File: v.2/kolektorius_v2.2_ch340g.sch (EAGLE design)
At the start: 87 parts, among them IC1 LM1117-33, IC2 ENC28J60, K1 G5V1, K2 G5V1, K3 G5V1, T1 2N2222, T2 2N2222, T3 2N2222, T4 2N2222, U1 ATMEGA328P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

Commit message: Paliktos 2 reles
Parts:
- removed D1: (no value), adafruit:DIODEDO-1N4148
- removed K1: G5V1, relay:G5V1
- removed LED1: (no value), adafruit:LEDSMT1206
- removed R5: 470, rcl:R-EU_R0805
- removed R6: 3k3, rcl:R-EU_R0805
- removed T2: 2N2222, adafruit:2N2222
- removed X8: 22-23-2031, con-molex:22-23-2031
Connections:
- net D+ renamed N$15
- net D- renamed N$11
- removed net D0: R6.2, U1.PD0(RXD)
- removed net N$11 (its old number): D1.A, K11.2, R5.2, T2.C
- removed net N$15 (its old number): K12.S, X8-1.S
- removed net N$17: R6.1, T2.B
- removed net N$28: K12.P, K12.P@1, X8-3.S
- removed net N$29: K12.O, X8-2.S
- removed net N$31: LED1.C, R5.1
- removed net N$51: U$2.RXD
- new net RXD: U1.PD0(RXD)
- new net TXD: U$2.RXD, U1.PD1(TXD)
- net +5V: no longer D1.C, K11.1, LED1.A
- net D1: no longer U1.PD1(TXD)
- net GND: no longer T2.E
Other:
- moved on the sheet: C13, C15, C17, USB

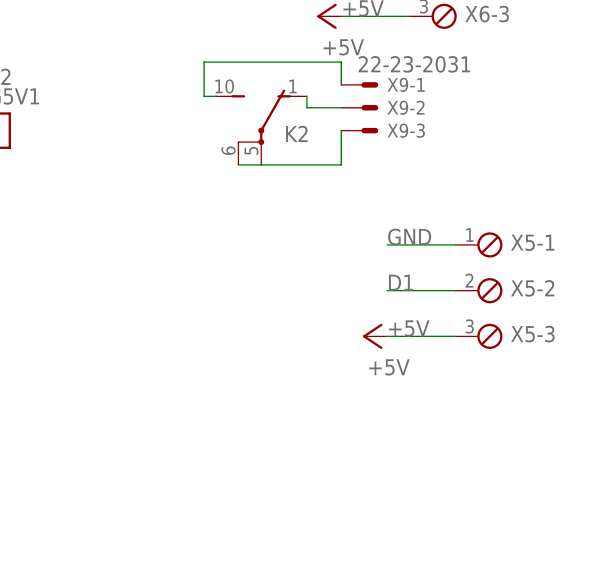
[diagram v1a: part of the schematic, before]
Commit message: pataisymai, paliktos 2 reles
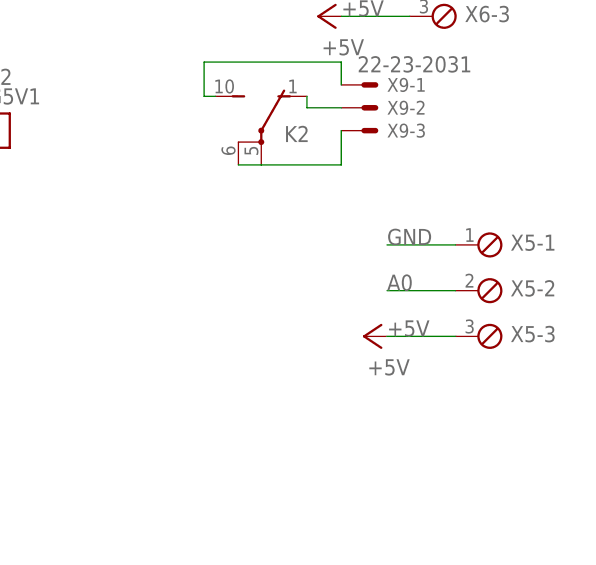
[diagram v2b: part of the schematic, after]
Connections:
- removed net D1: X5-2.1
- net A0: now also X5-2.1
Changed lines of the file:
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@@
 <label x="213.36" y="113.03" size="1.778" layer="95"/>
+</segment>
+<segment>
+<pinref part="X5" gate="-2" pin="1"/>
+<wire x1="313.69" y1="5.08" x2="306.07" y2="5.08" width="0.1524" layer="91"/>
+<label x="306.07" y="5.08" size="1.778" layer="95"/>
 </segment>
 </net>
@@
 </segment>
 </net>
-<net name="D1" class="0">
-<segment>
-<pinref part="X5" gate="-2" pin="1"/>
-<wire x1="313.69" y1="5.08" x2="306.07" y2="5.08" width="0.1524" layer="91"/>
-<label x="306.07" y="5.08" size="1.778" layer="95"/>
-</segment>
-</net>

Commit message: pataisymai
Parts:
- added R18, R5, R6: 4k7, rcl:R-EU_R0805
- added U$3: RELAYPTH, SRD-05VDC-SL-C:RELAYPTH
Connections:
- net +5V: now also R18.1, R5.1, R6.1
- net A0: now also R18.2
- net A1: now also R6.2
- net D2: now also R5.2
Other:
- moved on the sheet: K2, K3, X10-1, X10-2, X10-3, X9-1, X9-2, X9-3
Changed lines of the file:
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@@
 <layer number="97" name="Info" color="7" fill="1" visible="yes" active="yes"/>
 <layer number="98" name="Guide" color="6" fill="1" visible="yes" active="yes"/>
+<layer number="99" name="SpiceOrder" color="7" fill="1" visible="yes" active="yes"/>
 <layer number="100" name="Muster" color="7" fill="1" visible="no" active="no"/>
 <layer number="101" name="Patch_Top" color="12" fill="4" visible="yes" active="yes"/>
@@
 <part name="C17" library="rcl" deviceset="C-US" device="C0805K"/>
 <part name="+3V8" library="supply1" deviceset="+5V" device=""/>
+<part name="R5" library="rcl" deviceset="R-EU_" device="R0805" value="4k7"/>
+<part name="R6" library="rcl" deviceset="R-EU_" device="R0805" value="4k7"/>
+<part name="R18" library="rcl" deviceset="R-EU_" device="R0805" value="4k7"/>
+<part name="U$3" library="SRD-05VDC-SL-C" deviceset="RELAY" device="PTH"/>
 </parts>
 <sheets>
@@
 <instance part="GND11" gate="1" x="137.16" y="86.36"/>
 <instance part="K3" gate="1" x="260.35" y="59.69"/>
-<instance part="K3" gate="2" x="292.1" y="58.42"/>
+<instance part="K3" gate="2" x="276.86" y="57.15"/>
 <instance part="T4" gate="G$1" x="248.92" y="49.53" smashed="yes">
 <attribute name="NAME" x="251.46" y="50.8" size="1.778" layer="95"/>
@@
 <instance part="GND12" gate="1" x="251.46" y="41.91"/>
 <instance part="K2" gate="1" x="260.35" y="22.86"/>
-<instance part="K2" gate="2" x="292.1" y="21.59"/>
+<instance part="K2" gate="2" x="275.59" y="20.32"/>
 <instance part="T3" gate="G$1" x="248.92" y="12.7" smashed="yes">
 <attribute name="NAME" x="251.46" y="13.97" size="1.778" layer="95"/>
@@
 </instance>
 <instance part="GND18" gate="1" x="139.7" y="162.56"/>
-<instance part="X9" gate="-1" x="303.53" y="27.94"/>
-<instance part="X9" gate="-2" x="303.53" y="25.4"/>
-<instance part="X9" gate="-3" x="303.53" y="22.86"/>
-<instance part="X10" gate="-1" x="303.53" y="64.77"/>
-<instance part="X10" gate="-2" x="303.53" y="62.23"/>
-<instance part="X10" gate="-3" x="303.53" y="59.69"/>
+<instance part="X9" gate="-1" x="287.02" y="26.67"/>
+<instance part="X9" gate="-2" x="287.02" y="24.13"/>
+<instance part="X9" gate="-3" x="287.02" y="21.59"/>
+<instance part="X10" gate="-1" x="288.29" y="63.5"/>
+<instance part="X10" gate="-2" x="288.29" y="60.96"/>
+<instance part="X10" gate="-3" x="288.29" y="58.42"/>
 <instance part="X4" gate="-1" x="231.14" y="102.87"/>
 <instance part="X4" gate="-2" x="231.14" y="97.79"/>
@@
 <attribute name="VALUE" x="116.84" y="195.58" size="1.778" layer="96"/>
 </instance>
-<instance part="+3V14" gate="1" x="298.45" y="35.56" rot="R90"/>
-<instance part="+3V15" gate="1" x="303.53" y="0" rot="R90"/>
-<instance part="+3V16" gate="1" x="303.53" y="74.93" rot="R90"/>
+<instance part="+3V14" gate="1" x="285.75" y="35.56" rot="R90"/>
+<instance part="+3V15" gate="1" x="289.56" y="0" rot="R90"/>
+<instance part="+3V16" gate="1" x="290.83" y="74.93" rot="R90"/>
 <instance part="+3V17" gate="1" x="53.34" y="128.27" rot="R90"/>
 <instance part="R21" gate="G$1" x="128.27" y="170.18" smashed="yes" rot="R180">
@@
 <attribute name="VALUE" x="105.41" y="-19.05" size="1.778" layer="96" rot="R180"/>
 </instance>
+<instance part="R5" gate="G$1" x="300.99" y="80.01" smashed="yes">
+<attribute name="NAME" x="300.736" y="82.8294" size="1.778" layer="95" rot="R180"/>
+<attribute name="VALUE" x="303.276" y="78.74" size="1.778" layer="96" rot="R180"/>
+</instance>
+<instance part="R6" gate="G$1" x="295.91" y="40.64" smashed="yes">
+<attribute name="NAME" x="295.656" y="43.4594" size="1.778" layer="95" rot="R180"/>
+<attribute name="VALUE" x="298.196" y="39.37" size="1.778" layer="96" rot="R180"/>
+</instance>
+<instance part="R18" gate="G$1" x="300.99" y="5.08" smashed="yes">
+<attribute name="NAME" x="300.736" y="7.8994" size="1.778" layer="95" rot="R180"/>
+<attribute name="VALUE" x="303.276" y="3.81" size="1.778" layer="96" rot="R180"/>
+</instance>
+<instance part="U$3" gate="G$1" x="203.2" y="-17.78"/>
 </instances>
 <busses>
@@
 <wire x1="313.69" y1="5.08" x2="306.07" y2="5.08" width="0.1524" layer="91"/>
 <label x="306.07" y="5.08" size="1.778" layer="95"/>
+<pinref part="R18" gate="G$1" pin="2"/>
 </segment>
 </net>
@@
 <wire x1="308.61" y1="40.64" x2="300.99" y2="40.64" width="0.1524" layer="91"/>
 <label x="300.99" y="40.64" size="1.778" layer="95"/>
+<pinref part="R6" gate="G$1" pin="2"/>
 </segment>
 </net>
@@
 <pinref part="K3" gate="2" pin="P@1"/>
 <pinref part="K3" gate="2" pin="P"/>
-<wire x1="292.1" y1="55.88" x2="289.56" y2="55.88" width="0.1524" layer="91"/>
-<wire x1="300.99" y1="59.69" x2="300.99" y2="55.88" width="0.1524" layer="91"/>
-<wire x1="300.99" y1="55.88" x2="292.1" y2="55.88" width="0.1524" layer="91"/>
+<wire x1="276.86" y1="54.61" x2="274.32" y2="54.61" width="0.1524" layer="91"/>
+<wire x1="285.75" y1="58.42" x2="285.75" y2="54.61" width="0.1524" layer="91"/>
+<wire x1="285.75" y1="54.61" x2="276.86" y2="54.61" width="0.1524" layer="91"/>
 <pinref part="X10" gate="-3" pin="S"/>
 </segment>
@@
 <net name="N$20" class="1">
 <segment>
-<wire x1="300.99" y1="62.23" x2="297.18" y2="62.23" width="0.1524" layer="91"/>
+<wire x1="285.75" y1="60.96" x2="281.94" y2="60.96" width="0.1524" layer="91"/>
 <pinref part="K3" gate="2" pin="O"/>
-<wire x1="297.18" y1="62.23" x2="297.18" y2="63.5" width="0.1524" layer="91"/>
+<wire x1="281.94" y1="60.96" x2="281.94" y2="62.23" width="0.1524" layer="91"/>
 <pinref part="X10" gate="-2" pin="S"/>
 </segment>
@@
 <pinref part="K2" gate="2" pin="P@1"/>
 <pinref part="K2" gate="2" pin="P"/>
-<wire x1="292.1" y1="19.05" x2="289.56" y2="19.05" width="0.1524" layer="91"/>
-<wire x1="300.99" y1="22.86" x2="300.99" y2="19.05" width="0.1524" layer="91"/>
-<wire x1="300.99" y1="19.05" x2="292.1" y2="19.05" width="0.1524" layer="91"/>
+<wire x1="275.59" y1="17.78" x2="273.05" y2="17.78" width="0.1524" layer="91"/>
+<wire x1="284.48" y1="21.59" x2="284.48" y2="17.78" width="0.1524" layer="91"/>
+<wire x1="284.48" y1="17.78" x2="275.59" y2="17.78" width="0.1524" layer="91"/>
 <pinref part="X9" gate="-3" pin="S"/>
 </segment>
@@
 <net name="N$5" class="1">
 <segment>
-<wire x1="300.99" y1="25.4" x2="297.18" y2="25.4" width="0.1524" layer="91"/>
+<wire x1="284.48" y1="24.13" x2="280.67" y2="24.13" width="0.1524" layer="91"/>
 <pinref part="K2" gate="2" pin="O"/>
-<wire x1="297.18" y1="25.4" x2="297.18" y2="26.67" width="0.1524" layer="91"/>
+<wire x1="280.67" y1="24.13" x2="280.67" y2="25.4" width="0.1524" layer="91"/>
 <pinref part="X9" gate="-2" pin="S"/>
 </segment>
@@
 <segment>
 <pinref part="X7" gate="-2" pin="1"/>
+<pinref part="R5" gate="G$1" pin="2"/>
 <wire x1="313.69" y1="80.01" x2="306.07" y2="80.01" width="0.1524" layer="91"/>
 <label x="306.07" y="80.01" size="1.778" layer="95"/>
@@
 <segment>
 <pinref part="X9" gate="-1" pin="S"/>
-<wire x1="300.99" y1="27.94" x2="300.99" y2="30.48" width="0.1524" layer="91"/>
-<wire x1="300.99" y1="30.48" x2="285.75" y2="30.48" width="0.1524" layer="91"/>
-<wire x1="285.75" y1="30.48" x2="285.75" y2="26.67" width="0.1524" layer="91"/>
+<wire x1="284.48" y1="26.67" x2="284.48" y2="29.21" width="0.1524" layer="91"/>
+<wire x1="284.48" y1="29.21" x2="269.24" y2="29.21" width="0.1524" layer="91"/>
+<wire x1="269.24" y1="29.21" x2="269.24" y2="25.4" width="0.1524" layer="91"/>
 <pinref part="K2" gate="2" pin="S"/>
-<wire x1="285.75" y1="26.67" x2="287.02" y2="26.67" width="0.1524" layer="91"/>
+<wire x1="269.24" y1="25.4" x2="270.51" y2="25.4" width="0.1524" layer="91"/>
 </segment>
 </net>
@@
 <segment>
 <pinref part="X10" gate="-1" pin="S"/>
-<wire x1="300.99" y1="64.77" x2="300.99" y2="67.31" width="0.1524" layer="91"/>
-<wire x1="300.99" y1="67.31" x2="285.75" y2="67.31" width="0.1524" layer="91"/>
-<wire x1="285.75" y1="67.31" x2="285.75" y2="63.5" width="0.1524" layer="91"/>
+<wire x1="285.75" y1="63.5" x2="285.75" y2="66.04" width="0.1524" layer="91"/>
+<wire x1="285.75" y1="66.04" x2="270.51" y2="66.04" width="0.1524" layer="91"/>
+<wire x1="270.51" y1="66.04" x2="270.51" y2="62.23" width="0.1524" layer="91"/>
 <pinref part="K3" gate="2" pin="S"/>
-<wire x1="285.75" y1="63.5" x2="287.02" y2="63.5" width="0.1524" layer="91"/>
+<wire x1="270.51" y1="62.23" x2="271.78" y2="62.23" width="0.1524" layer="91"/>
 </segment>
 </net>
@@
 <segment>
 <pinref part="X6" gate="-3" pin="1"/>
-<wire x1="308.61" y1="35.56" x2="300.99" y2="35.56" width="0.1524" layer="91"/>
+<wire x1="308.61" y1="35.56" x2="290.83" y2="35.56" width="0.1524" layer="91"/>
 <label x="300.99" y="35.56" size="1.778" layer="95"/>
 <pinref part="+3V14" gate="1" pin="+5V"/>
+<pinref part="R6" gate="G$1" pin="1"/>
+<wire x1="290.83" y1="35.56" x2="288.29" y2="35.56" width="0.1524" layer="91"/>
+<wire x1="290.83" y1="40.64" x2="290.83" y2="35.56" width="0.1524" layer="91"/>
+<junction x="290.83" y="35.56"/>
 </segment>
 <segment>
 <pinref part="X5" gate="-3" pin="1"/>
-<wire x1="313.69" y1="0" x2="306.07" y2="0" width="0.1524" layer="91"/>
+<wire x1="313.69" y1="0" x2="295.91" y2="0" width="0.1524" layer="91"/>
 <label x="306.07" y="0" size="1.778" layer="95"/>
 <pinref part="+3V15" gate="1" pin="+5V"/>
+<pinref part="R18" gate="G$1" pin="1"/>
+<wire x1="295.91" y1="0" x2="292.1" y2="0" width="0.1524" layer="91"/>
+<wire x1="295.91" y1="5.08" x2="295.91" y2="0" width="0.1524" layer="91"/>
+<junction x="295.91" y="0"/>
 </segment>
 <segment>
 <pinref part="X7" gate="-3" pin="1"/>
-<wire x1="313.69" y1="74.93" x2="306.07" y2="74.93" width="0.1524" layer="91"/>
+<wire x1="313.69" y1="74.93" x2="295.91" y2="74.93" width="0.1524" layer="91"/>
 <label x="306.07" y="74.93" size="1.778" layer="95"/>
 <pinref part="+3V16" gate="1" pin="+5V"/>
-</segment>
-<segment>
+<pinref part="R5" gate="G$1" pin="1"/>
+<wire x1="295.91" y1="74.93" x2="293.37" y2="74.93" width="0.1524" layer="91"/>
+<wire x1="295.91" y1="80.01" x2="295.91" y2="74.93" width="0.1524" layer="91"/>
+<junction x="295.91" y="74.93"/>
+</segment>
+<segment>

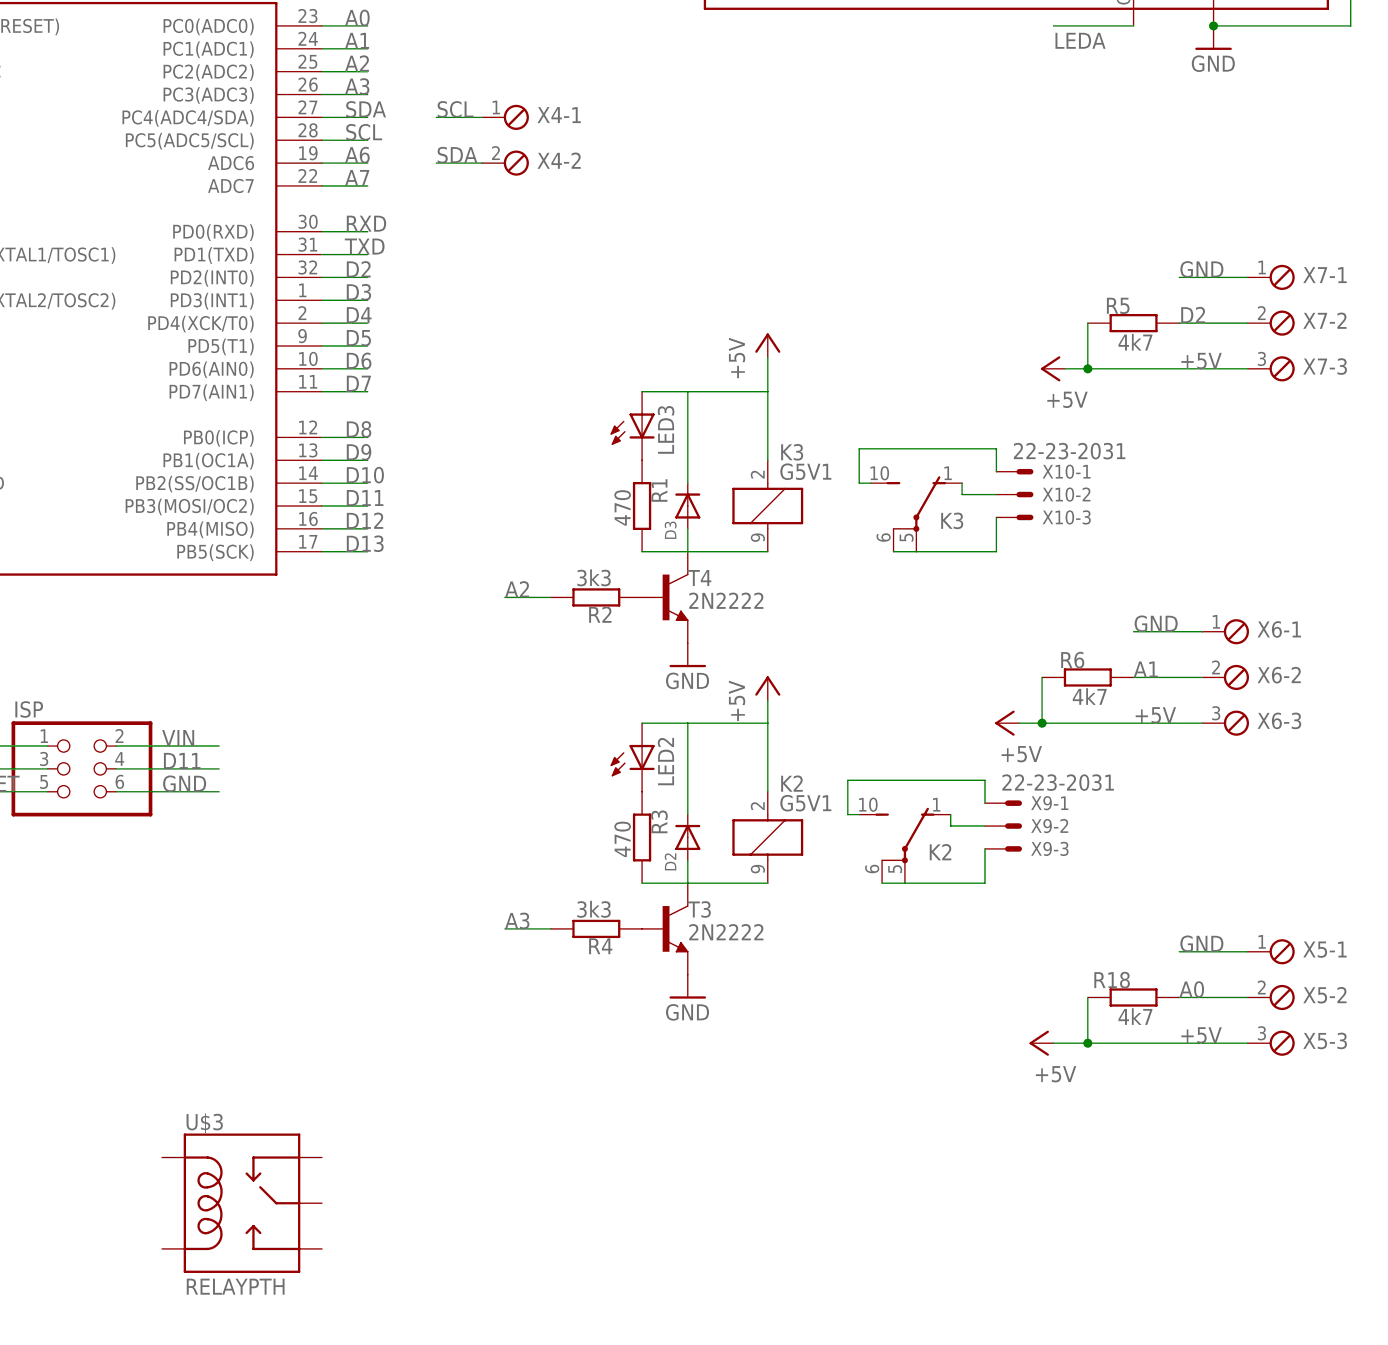
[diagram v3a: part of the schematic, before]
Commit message: pataisymai
2 reles jrc-21f(4100)
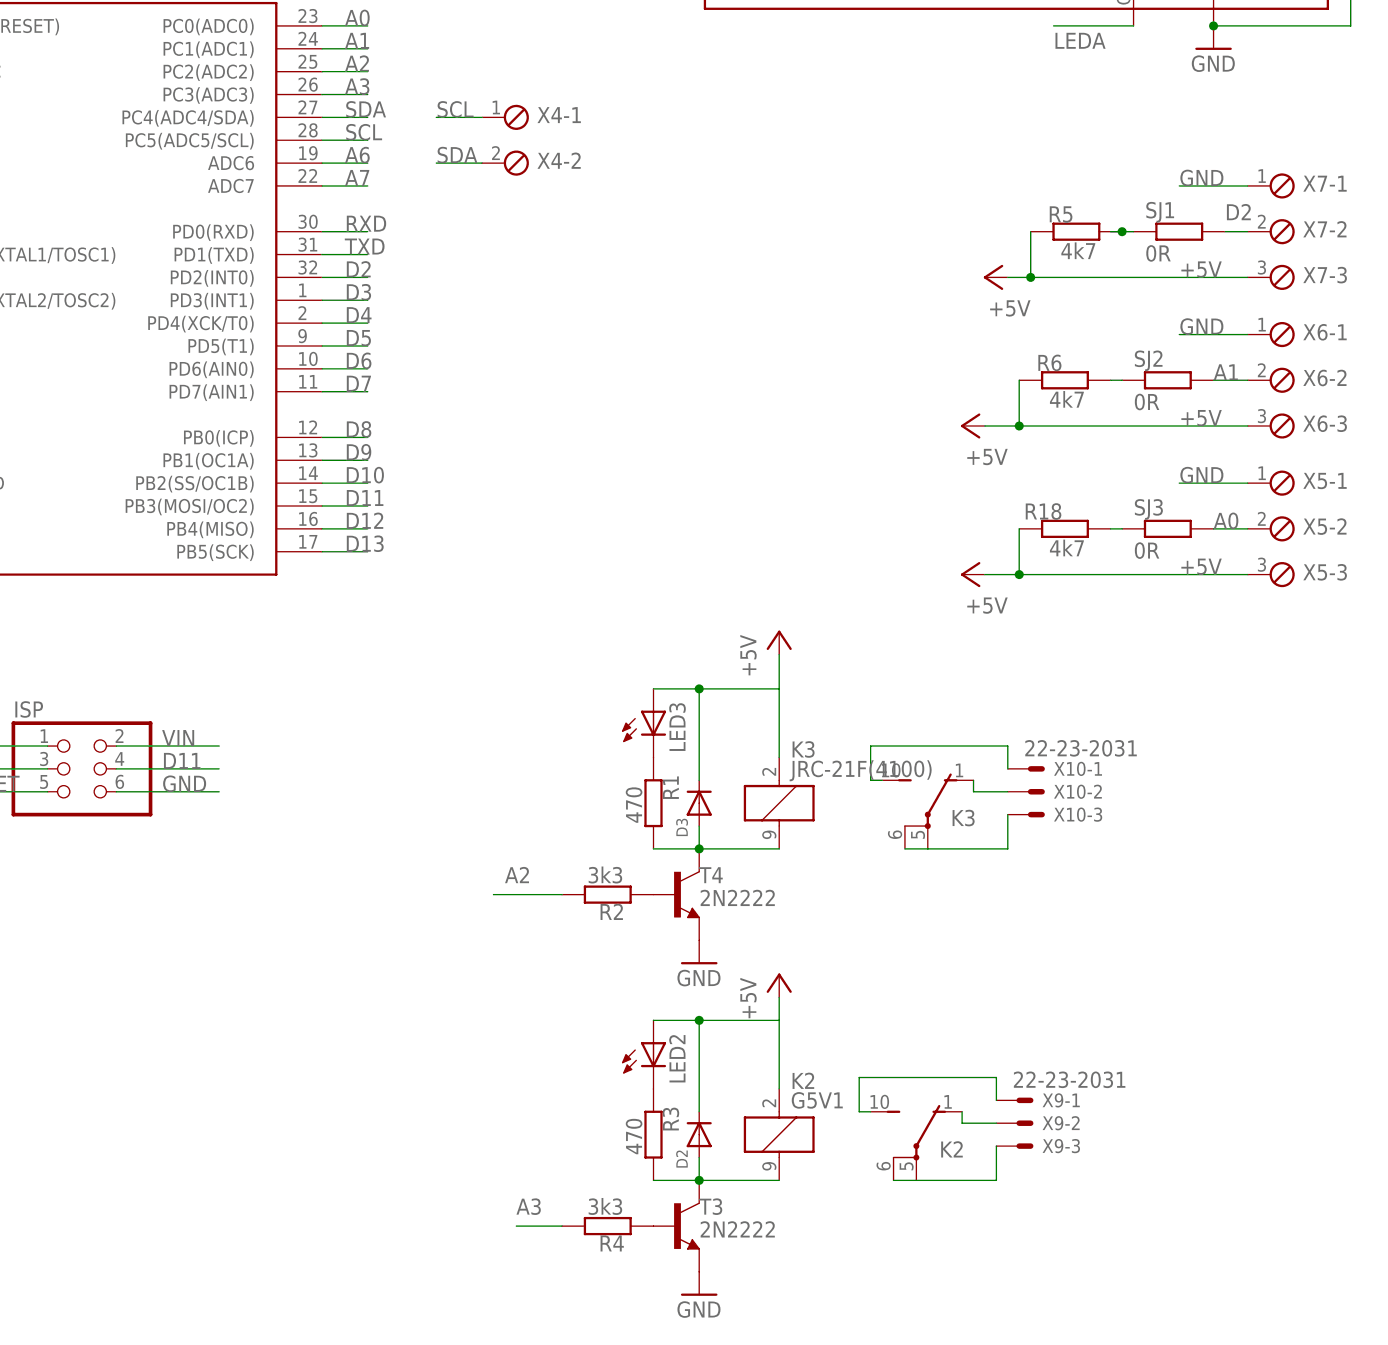
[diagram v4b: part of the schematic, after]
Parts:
- removed U$3: RELAYPTH, SRD-05VDC-SL-C:RELAYPTH
- added SJ1, SJ2, SJ3: 0R, rcl:R-EU_R0201
- K3: value G5V1 -> JRC-21F(4100); device relay:G5V1 -> relay:JRC-21F(4100)
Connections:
- removed net N$27: LED3.A
- new net N$17: R6.2, SJ2.1
- new net N$28: R18.2, SJ3.1
- new net N$31: R5.2, SJ1.1
- net +5V: now also LED3.A
- net A0: now also SJ3.2; no longer R18.2
- net A1: now also SJ2.2; no longer R6.2
- net D2: now also SJ1.2; no longer R5.2
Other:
- moved on the sheet: D2, D3, K2, K3, LED2, LED3, R1, R18, R2, R3, R4, R5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
